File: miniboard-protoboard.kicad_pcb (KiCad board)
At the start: 2 copper layers, 50.8 x 50.8 mm, 508 parts

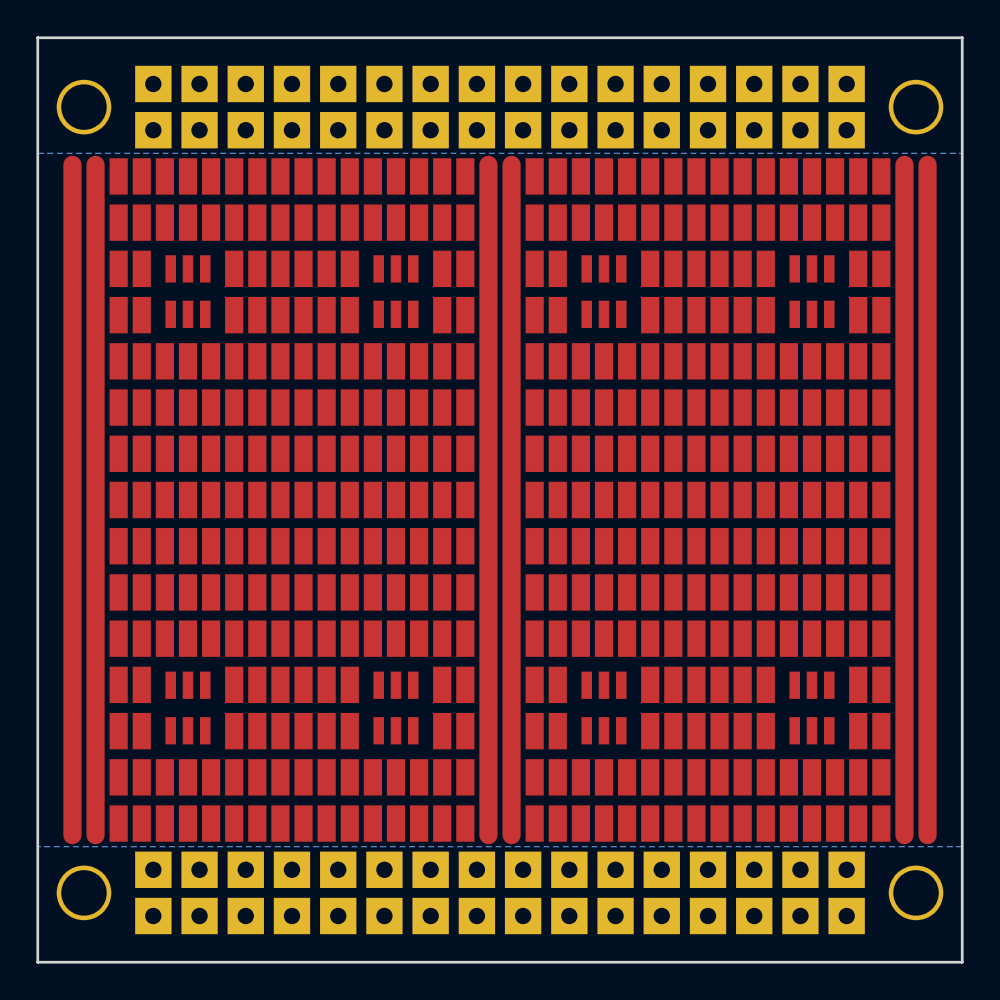
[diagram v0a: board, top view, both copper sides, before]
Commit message: remove solder mask over traces
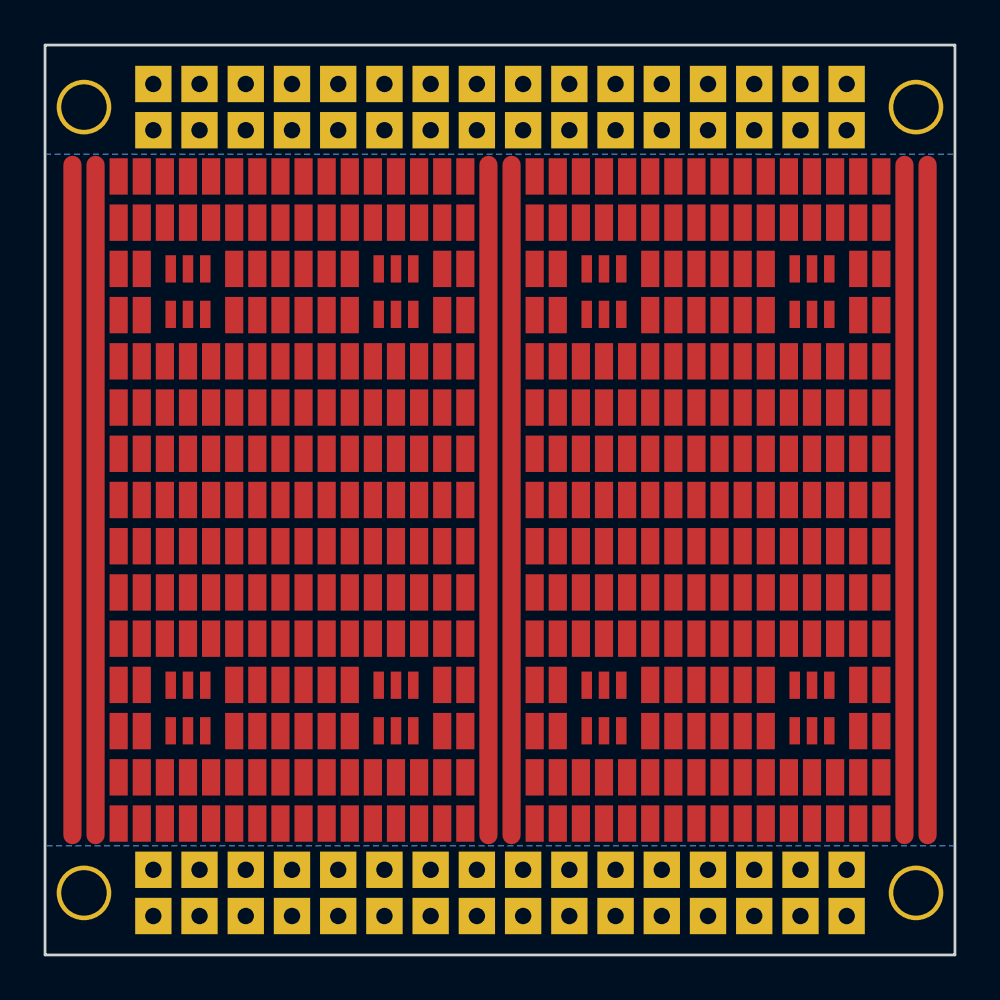
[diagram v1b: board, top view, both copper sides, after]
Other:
- board size 50.8 x 50.8 mm -> 50 x 50 mm
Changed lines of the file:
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@@
-(kicad_pcb (version 4) (host pcbnew 0.201602201416+6573~42~ubuntu14.04.1-product)
+(kicad_pcb (version 4) (host pcbnew 0.201603031449+6606~43~ubuntu14.04.1-product)
   (general
     (links 0)
@@
     (pad_drill 0.762)
     (pad_to_mask_clearance 0.2)
-    (aux_axis_origin 0 0)
+    (aux_axis_origin 177.8 101.6)
+    (grid_origin 177.8 101.6)
     (visible_elements FFFFFF7F)
     (pcbplotparams
@@
       (solder_mask_margin 1) (clearance 1))
   )
-  (gr_line (start 152.4 127) (end 152.4 76.2) (layer Edge.Cuts) (width 0.15))
-  (gr_line (start 203.2 127) (end 152.4 127) (layer Edge.Cuts) (width 0.15))
-  (gr_line (start 203.2 76.2) (end 203.2 127) (layer Edge.Cuts) (width 0.15))
-  (gr_line (start 152.4 76.2) (end 203.2 76.2) (layer Edge.Cuts) (width 0.15))
-  (dimension 50.8 (width 0.3) (layer Dwgs.User)
-    (gr_text "50,800 mm" (at 236.3 101.6 270) (layer Dwgs.User)
+  (gr_line (start 152.8 126.6) (end 152.8 76.6) (layer Edge.Cuts) (width 0.15))
+  (gr_line (start 202.8 126.6) (end 152.8 126.6) (layer Edge.Cuts) (width 0.15))
+  (gr_line (start 202.8 76.6) (end 202.8 126.6) (layer Edge.Cuts) (width 0.15))
+  (gr_line (start 152.8 76.6) (end 202.8 76.6) (layer Edge.Cuts) (width 0.15))
+  (dimension 50 (width 0.3) (layer Dwgs.User)
+    (gr_text "50,000 mm" (at 236.139251 101.6 270) (layer Dwgs.User)
       (effects (font (size 1.5 1.5) (thickness 0.3)))
     )
-    (feature1 (pts (xy 208.28 127) (xy 237.65 127)))
-    (feature2 (pts (xy 208.28 76.2) (xy 237.65 76.2)))
-    (crossbar (pts (xy 234.95 76.2) (xy 234.95 127)))
-    (arrow1a (pts (xy 234.95 127) (xy 234.363579 125.873496)))
-    (arrow1b (pts (xy 234.95 127) (xy 235.536421 125.873496)))
-    (arrow2a (pts (xy 234.95 76.2) (xy 234.363579 77.326504)))
-    (arrow2b (pts (xy 234.95 76.2) (xy 235.536421 77.326504)))
+    (feature1 (pts (xy 207.8 126.6) (xy 237.489251 126.6)))
+    (feature2 (pts (xy 207.8 76.6) (xy 237.489251 76.6)))
+    (crossbar (pts (xy 234.789251 76.6) (xy 234.789251 126.6)))
+    (arrow1a (pts (xy 234.789251 126.6) (xy 234.20283 125.473496)))
+    (arrow1b (pts (xy 234.789251 126.6) (xy 235.375672 125.473496)))
+    (arrow2a (pts (xy 234.789251 76.6) (xy 234.20283 77.726504)))
+    (arrow2b (pts (xy 234.789251 76.6) (xy 235.375672 77.726504)))
   )
-  (dimension 50.8 (width 0.3) (layer Dwgs.User)
-    (gr_text "50,800 mm" (at 177.8 58.34) (layer Dwgs.User)
+  (dimension 50 (width 0.3) (layer Dwgs.User)
+    (gr_text "50,000 mm" (at 177.8 58.55) (layer Dwgs.User)
       (effects (font (size 1.5 1.5) (thickness 0.3)))
     )
-    (feature1 (pts (xy 203.2 72.39) (xy 203.2 56.99)))
-    (feature2 (pts (xy 152.4 72.39) (xy 152.4 56.99)))
-    (crossbar (pts (xy 152.4 59.69) (xy 203.2 59.69)))
-    (arrow1a (pts (xy 203.2 59.69) (xy 202.073496 60.276421)))
-    (arrow1b (pts (xy 203.2 59.69) (xy 202.073496 59.103579)))
-    (arrow2a (pts (xy 152.4 59.69) (xy 153.526504 60.276421)))
-    (arrow2b (pts (xy 152.4 59.69) (xy 153.526504 59.103579)))
+    (feature1 (pts (xy 202.8 72.6) (xy 202.8 57.2)))
+    (feature2 (pts (xy 152.8 72.6) (xy 152.8 57.2)))
+    (crossbar (pts (xy 152.8 59.9) (xy 202.8 59.9)))
+    (arrow1a (pts (xy 202.8 59.9) (xy 201.673496 60.486421)))
+    (arrow1b (pts (xy 202.8 59.9) (xy 201.673496 59.313579)))
+    (arrow2a (pts (xy 152.8 59.9) (xy 153.926504 60.486421)))
+    (arrow2b (pts (xy 152.8 59.9) (xy 153.926504 59.313579)))
   )
   (segment (start 154.305 83.185) (end 154.305 120.015) (width 1) (layer F.Cu) (net 0))
@@
     (polygon
       (pts
-        (xy 152.4 82.55) (xy 203.2 82.55) (xy 203.2 120.65) (xy 152.4 120.65)
+        (xy 152.8 82.6) (xy 202.8 82.6) (xy 202.8 120.6) (xy 152.8 120.6)
+      )
+    )
+  )
+  (zone (net 0) (net_name "") (layer F.Mask) (hatch edge 0.508)
+    (connect_pads (clearance 0.508))
+    (min_thickness 0.254)
+    (fill yes (arc_segments 16) (thermal_gap 0.508) (thermal_bridge_width 0.508))
+    (polygon
+      (pts
+        (xy 153.67 82.55) (xy 156.21 82.55) (xy 156.21 120.65) (xy 153.67 120.65)
+      )
+    )
+  )
+  (zone (net 0) (net_name "") (layer F.Mask) (hatch edge 0.508)
+    (connect_pads (clearance 0.508))
+    (min_thickness 0.254)
+    (fill yes (arc_segments 16) (thermal_gap 0.508) (thermal_bridge_width 0.508))
+    (polygon
+      (pts
+        (xy 176.53 82.55) (xy 179.07 82.55) (xy 179.07 120.65) (xy 176.53 120.65)
+      )
+    )
+  )
+  (zone (net 0) (net_name "") (layer F.Mask) (hatch edge 0.508)
+    (connect_pads (clearance 0.508))
+    (min_thickness 0.254)
+    (fill yes (arc_segments 16) (thermal_gap 0.508) (thermal_bridge_width 0.508))
+    (polygon
+      (pts
+        (xy 199.39 82.55) (xy 201.93 82.55) (xy 201.93 120.65) (xy 199.39 120.65)
       )
     )
